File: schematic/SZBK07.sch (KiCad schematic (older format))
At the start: 25 parts, among them Q1 2N3904, Q2 2N3904, Q3 IRFZ44N, U1 SZBK07_DC-DC_module, U2 AD822A, U3 MP2307_DC-DC_module, U4 ArduinoNano

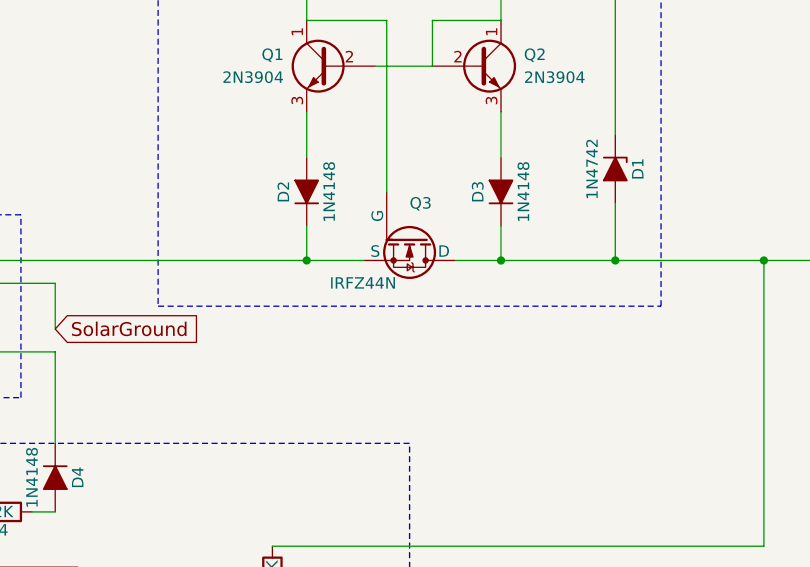
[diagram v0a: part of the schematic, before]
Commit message: corrected MOSFET to PSMN3R3-80PS
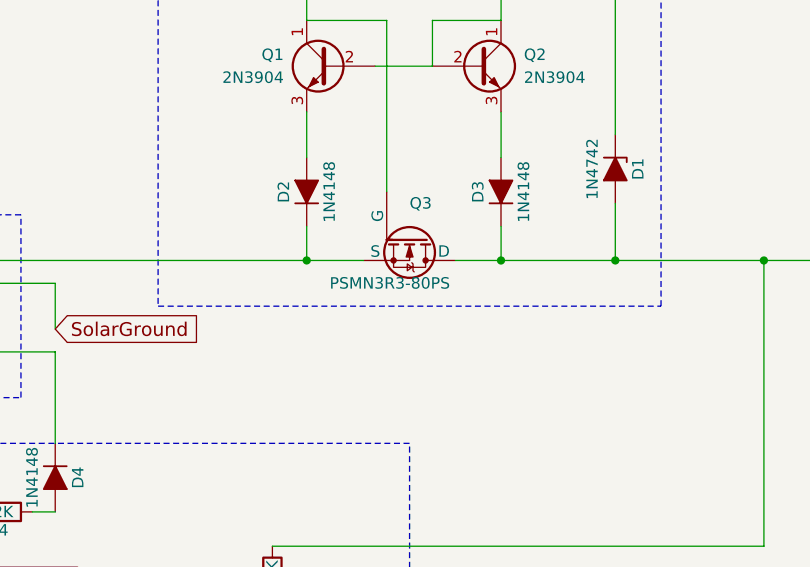
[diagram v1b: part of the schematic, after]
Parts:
- Q3: value IRFZ44N -> PSMN3R3-80PS
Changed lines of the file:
@@
 LIBS:contrib
 LIBS:valves
-LIBS:SZBK01-cache
+LIBS:SZBK07-cache
 EELAYER 25 0
 EELAYER END
@@
 P 6550 2700
 F 0 "Q3" V 6400 2700 50  0000 L CNN
-F 1 "IRFZ44N" V 6750 2350 50  0000 L CNN
+F 1 "PSMN3R3-80PS" V 6750 2350 50  0000 L CNN
 F 2 "TO-220" H 6750 2625 50  0001 L CIN
 F 3 "" H 6550 2700 50  0001 L CNN

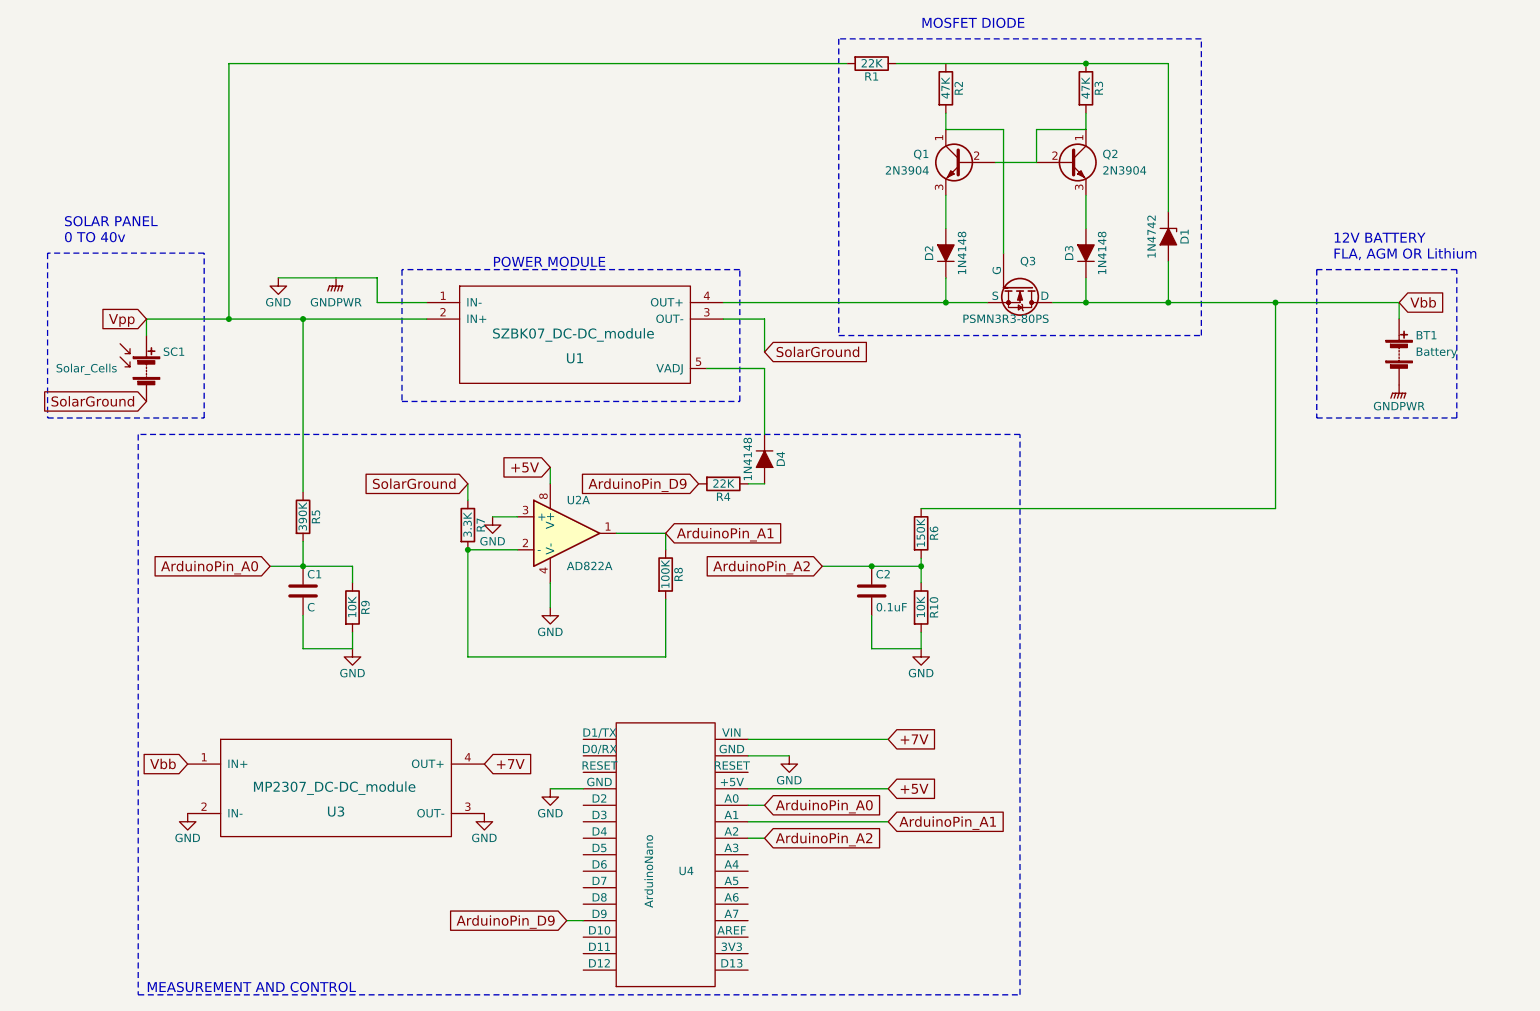
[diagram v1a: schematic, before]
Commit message: updated MOSFET diode circuit
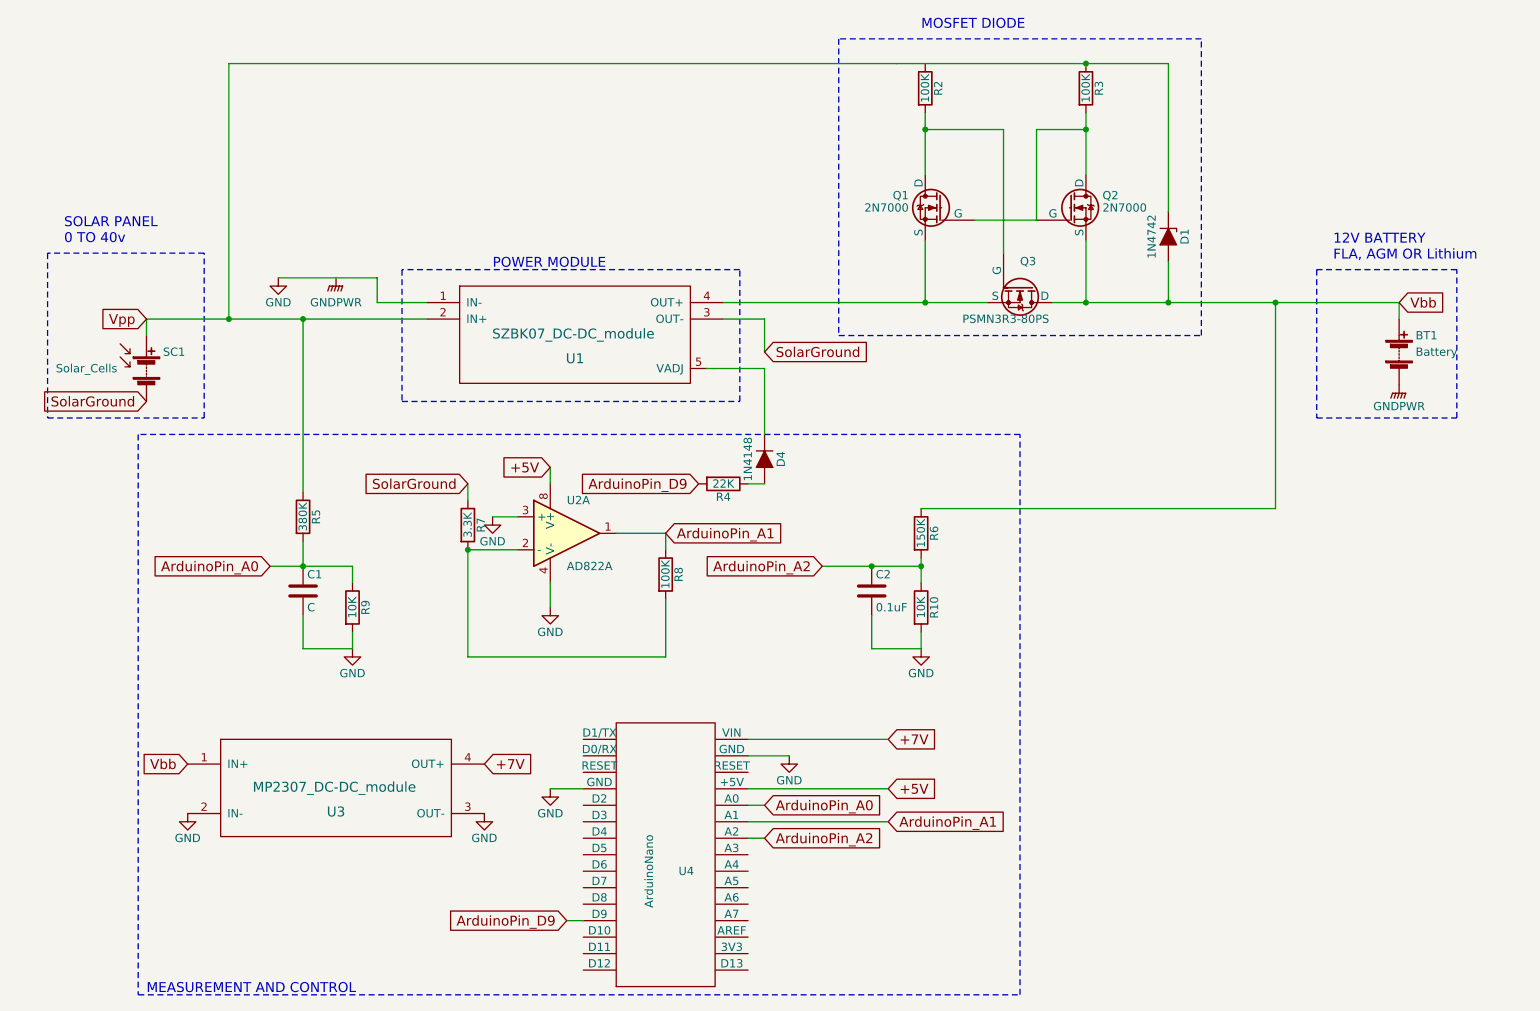
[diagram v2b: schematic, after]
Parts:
- removed D2, D3: 1N4148, symbol D_ALT
- removed Q1, Q2: 2N3904, symbol Q_NPN_CBE
- removed R1: 22K, symbol R
- added Q1, Q2: 2N7000, TO_SOT_Packages_THT:TO-92_Molded_Narrow, symbol 2N7000
- R2, R3: value 47K -> 100K
- R5: value 390K -> 380K
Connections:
- net Vbb: now also Q2.3 (S)
- net Vpp: now also D1.1 (K), R3.1
- net at Q3.3 (S), U1.4 (OUT+): now also Q1.3 (S)
- net at Q3.1 (G), R2.2: now also Q1.1 (D)
- net at R3.2: now also Q1.2 (G), Q2.1 (D), Q2.2 (G)
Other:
- moved on the sheet: R2
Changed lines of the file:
@@
 $EndComp
 $Comp
-L GNDPWR #PWR1
+L GNDPWR #PWR2
 U 1 1 5B485E0B
 P 2400 2650
-F 0 "#PWR1" H 2400 2450 50  0001 C CNN
+F 0 "#PWR2" H 2400 2450 50  0001 C CNN
 F 1 "GNDPWR" H 2400 2500 50  0000 C CNN
 F 2 "" H 2400 2600 50  0001 C CNN
@@
 $EndComp
 Wire Wire Line
-	4750 2800 6350 2800
+	4750 2800 5975 2800
+Wire Wire Line
+	5975 2800 6350 2800
 $Comp
 L Battery BT1
@@
 $EndComp
 $Comp
-L GNDPWR #PWR4
+L GNDPWR #PWR3
 U 1 1 5B485FBA
 P 8850 3300
-F 0 "#PWR4" H 8850 3100 50  0001 C CNN
+F 0 "#PWR3" H 8850 3100 50  0001 C CNN
 F 1 "GNDPWR" H 8850 3170 50  0000 C CNN
 F 2 "" H 8850 3250 50  0001 C CNN
@@
 	1    0    0    -1
 $EndComp
-$Comp
-L D_ALT D2
-U 1 1 5B486046
-P 6100 2500
-F 0 "D2" H 6100 2600 50  0000 C CNN
-F 1 "1N4148" H 6100 2400 50  0000 C CNN
-F 2 "" H 6100 2500 50  0001 C CNN
-F 3 "" H 6100 2500 50  0001 C CNN
-	1    6100 2500
-	0    -1   -1   0
-$EndComp
-Wire Wire Line
-	6100 2800 6100 2650
-$Comp
-L D_ALT D3
-U 1 1 5B486096
-P 6950 2500
-F 0 "D3" H 6950 2600 50  0000 C CNN
-F 1 "1N4148" H 6950 2400 50  0000 C CNN
-F 2 "" H 6950 2500 50  0001 C CNN
-F 3 "" H 6950 2500 50  0001 C CNN
-	1    6950 2500
-	0    -1   -1   0
-$EndComp
-Wire Wire Line
-	6950 2650 6950 2800
-$Comp
-L Q_NPN_CBE Q2
-U 1 1 5B4860E6
-P 6850 1950
-F 0 "Q2" H 7050 2000 50  0000 L CNN
-F 1 "2N3904" H 7050 1900 50  0000 L CNN
-F 2 "" H 7050 2050 50  0001 C CNN
-F 3 "" H 6850 1950 50  0001 C CNN
-	1    6850 1950
-	1    0    0    -1
-$EndComp
-Wire Wire Line
-	6950 2150 6950 2350
-$Comp
-L Q_NPN_CBE Q1
-U 1 1 5B486160
-P 6200 1950
-F 0 "Q1" H 6400 2000 50  0000 L CNN
-F 1 "2N3904" H 6400 1900 50  0000 L CNN
-F 2 "" H 6400 2050 50  0001 C CNN
-F 3 "" H 6200 1950 50  0001 C CNN
-	1    6200 1950
-	-1   0    0    -1
-$EndComp
-Wire Wire Line
-	6100 2150 6100 2350
-Wire Wire Line
-	6400 1950 6650 1950
-Wire Wire Line
-	6100 1750 6450 1750
+Wire Wire Line
+	5975 2800 5975 2425
+Wire Wire Line
+	6950 2425 6950 2800
+Wire Wire Line
+	5975 1750 6450 1750
 Wire Wire Line
 	6450 1750 6450 2500
@@
 	6950 1750 6650 1750
 Wire Wire Line
-	6650 1750 6650 1950
+	6650 1750 6650 2300
 $Comp
 L R R2
 U 1 1 5B4865B4
-P 6100 1500
-F 0 "R2" V 6180 1500 50  0000 C CNN
-F 1 "47K" V 6100 1500 50  0000 C CNN
-F 2 "" V 6030 1500 50  0001 C CNN
-F 3 "" H 6100 1500 50  0001 C CNN
-	1    6100 1500
-	1    0    0    -1
-$EndComp
-Wire Wire Line
-	6100 1650 6100 1750
+P 5975 1500
+F 0 "R2" V 6055 1500 50  0000 C CNN
+F 1 "100K" V 5975 1500 50  0000 C CNN
+F 2 "" V 5905 1500 50  0001 C CNN
+F 3 "" H 5975 1500 50  0001 C CNN
+	1    5975 1500
+	1    0    0    -1
+$EndComp
+Wire Wire Line
+	5975 1650 5975 1750
+Wire Wire Line
+	5975 1750 5975 2025
 $Comp
 L R R3
@@
 P 6950 1500
 F 0 "R3" V 7030 1500 50  0000 C CNN
-F 1 "47K" V 6950 1500 50  0000 C CNN
+F 1 "100K" V 6950 1500 50  0000 C CNN
 F 2 "" V 6880 1500 50  0001 C CNN
 F 3 "" H 6950 1500 50  0001 C CNN
@@
 	6950 1650 6950 1750
 Wire Wire Line
-	5800 1350 7450 1350
+	6950 1750 6950 2025
+Wire Wire Line
+	5800 1350 6950 1350
+Wire Wire Line
+	6950 1350 7450 1350
 $Comp
 L D_Zener_ALT D1
@@
 	7450 1350 7450 2250
 Connection ~ 6950 1350
-$Comp
-L R R1
-U 1 1 5B48679E
-P 5650 1350
-F 0 "R1" V 5730 1350 50  0000 C CNN
-F 1 "22K" V 5650 1350 50  0000 C CNN
-F 2 "" V 5580 1350 50  0001 C CNN
-F 3 "" H 5650 1350 50  0001 C CNN
-	1    5650 1350
-	0    1    1    0
-$EndComp
-Wire Wire Line
-	5500 1350 1750 1350
+Wire Wire Line
+	5800 1350 1750 1350
 Wire Wire Line
 	1750 1350 1750 2900
@@
 $EndComp
 $Comp
-L GND #PWR2
+L GND #PWR1
 U 1 1 5B488158
 P 2050 2650
-F 0 "#PWR2" H 2050 2400 50  0001 C CNN
+F 0 "#PWR1" H 2050 2400 50  0001 C CNN
 F 1 "GND" H 2050 2500 50  0000 C CNN
 F 2 "" H 2050 2650 50  0001 C CNN
@@
 P 2200 4100
 F 0 "R5" V 2280 4100 50  0000 C CNN
-F 1 "390K" V 2200 4100 50  0000 C CNN
+F 1 "380K" V 2200 4100 50  0000 C CNN
 F 2 "" V 2130 4100 50  0001 C CNN
 F 3 "" H 2200 4100 50  0001 C CNN
@@
 $EndComp
 Wire Wire Line
-	2000 4400 2500 4400
+	2000 4400 2200 4400
+Wire Wire Line
+	2200 4400 2500 4400
 Wire Wire Line
 	2200 4700 2200 4900
@@
 $EndComp
 Wire Wire Line
-	5950 4350 5950 4500
+	5950 4350 5950 4400
+Wire Wire Line
+	5950 4400 5950 4500
 Wire Wire Line
 	5950 4800 5950 4900
@@
 $EndComp
 Wire Wire Line
-	5350 4400 5950 4400
+	5350 4400 5650 4400
+Wire Wire Line
+	5650 4400 5950 4400
 Connection ~ 5950 4400
 Wire Wire Line
@@
 Wire Wire Line
 	3900 5750 3700 5750
-Connection ~ 6100 2800
-Wire Wire Line
-	6750 2800 8850 2800
+Connection ~ 5975 2800
+Wire Wire Line
+	6750 2800 6950 2800
+Wire Wire Line
+	6950 2800 7450 2800
+Wire Wire Line
+	7450 2800 8100 2800
+Wire Wire Line
+	8100 2800 8850 2800
 Connection ~ 6950 2800
 Connection ~ 7450 2800
@@
 	5000 2900 5000 3100
 Wire Wire Line
-	1250 2900 2950 2900
+	1250 2900 1750 2900
+Wire Wire Line
+	1750 2900 2200 2900
+Wire Wire Line
+	2200 2900 2950 2900
 Connection ~ 1750 2900
 Wire Wire Line
@@
 	2650 2800 2650 2650
 $Comp
-L GND #PWR?
+L GND #PWR4
 U 1 1 5B494DA1
 P 3350 4100
-F 0 "#PWR?" H 3350 3850 50  0001 C CNN
+F 0 "#PWR4" H 3350 3850 50  0001 C CNN
 F 1 "GND" H 3350 3950 50  0000 C CNN
 F 2 "" H 3350 4100 50  0001 C CNN
@@
 Text Notes 8450 2550 0    60   ~ 0
 12V BATTERY\nFLA, AGM OR Lithium
+$Comp
+L 2N7000 Q2
+U 1 1 5B5C69A6
+P 6850 2225
+F 0 "Q2" H 7050 2300 50  0000 L CNN
+F 1 "2N7000" H 7050 2225 50  0000 L CNN
+F 2 "TO_SOT_Packages_THT:TO-92_Molded_Narrow" H 7050 2150 50  0001 L CIN
+F 3 "" H 6850 2225 50  0001 L CNN
+	1    6850 2225
+	1    0    0    -1
+$EndComp
+$Comp
+L 2N7000 Q1
+U 1 1 5B5C6A55
+P 6075 2225
+F 0 "Q1" H 6275 2300 50  0000 L CNN
+F 1 "2N7000" H 6275 2225 50  0000 L CNN
+F 2 "TO_SOT_Packages_THT:TO-92_Molded_Narrow" H 6275 2150 50  0001 L CIN
+F 3 "" H 6075 2225 50  0001 L CNN
+	1    6075 2225
+	-1   0    0    -1
+$EndComp
+Connection ~ 6950 1750
+Wire Wire Line
+	6650 2300 6275 2300
+Connection ~ 5975 1750
 $EndSCHEMATC
